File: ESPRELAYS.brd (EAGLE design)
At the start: 47 x 78 mm, 52 parts, among them IC1 ESP12SMT, J1 2.1MM DC Jack, K1 HE751, K2 HE751, K3 HE751, K4 HE751, Q1 2N7002, Q2 2N7002, Q3 2N7002, Q4 2N7002

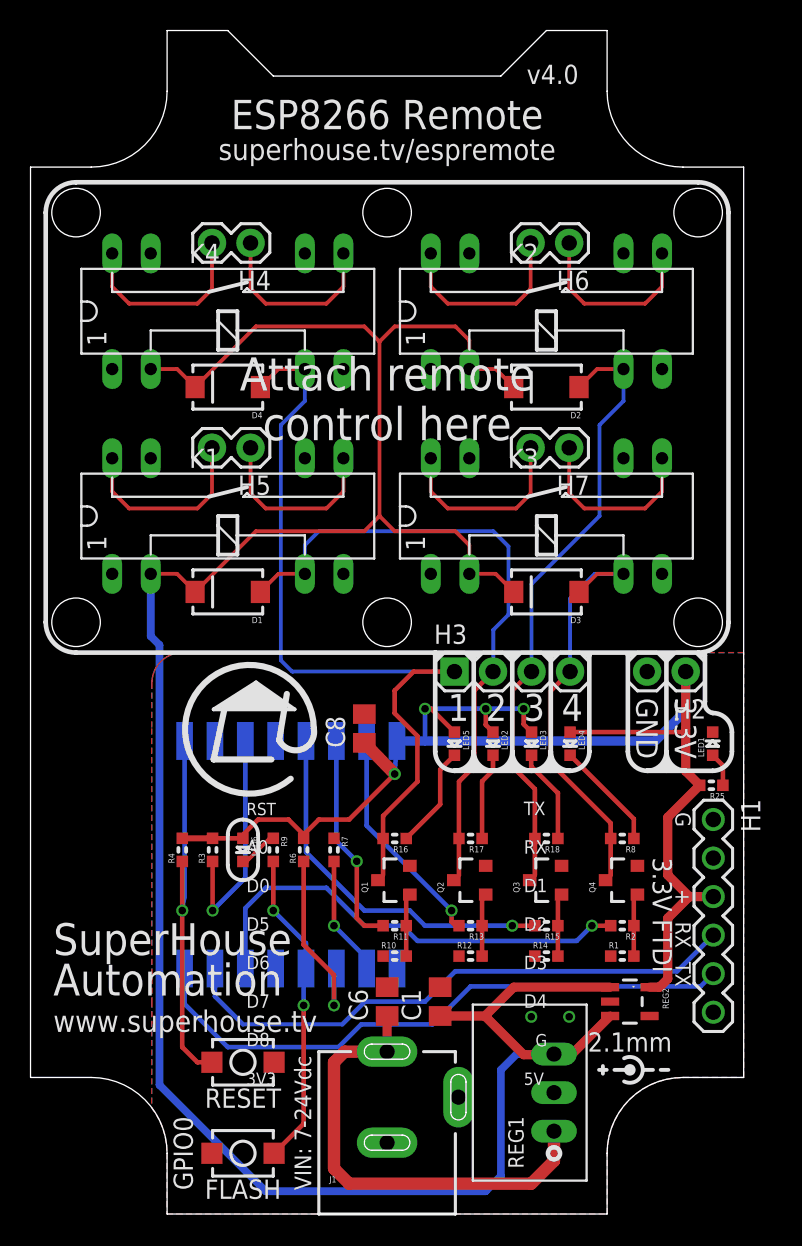
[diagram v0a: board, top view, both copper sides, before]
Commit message: Added SIP reed relays
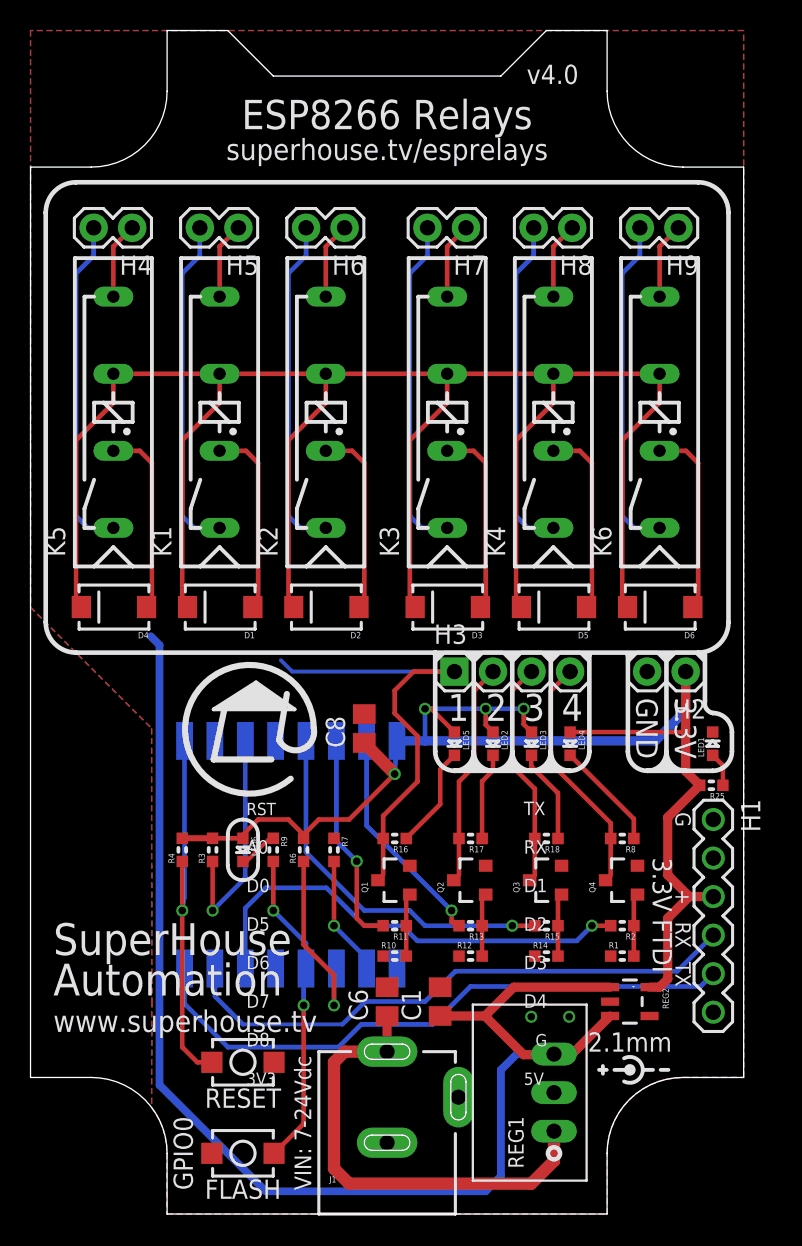
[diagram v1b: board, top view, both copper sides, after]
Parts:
- added D5, D6: (no value), SparkFun:SMA-DIODE
- added H8, H9: (no value), freetronics-jon:1X02
- added K5, K6: REED, relay:REED
- K1, K2, K3, K4: value HE751 -> REED; device relay:HE751 -> relay:REED
- moved K4 24.3 mm to (37.0, 63.0), turned to 90 degrees
- moved D2 20.5 mm to (19.5, 40.0)
- moved K3 17.5 mm to (30.0, 63.0), turned to 90 degrees
- moved K1 17.1 mm to (15.0, 63.0), turned to 90 degrees
- moved D4 16.3 mm to (5.50, 40.0)
- moved H7 16.0 mm to (28.7, 65.0)
- moved H6 14.8 mm to (20.7, 65.0)
- moved H5 14.5 mm to (13.7, 65.0)
- moved K2 12.5 mm to (22.0, 63.0), turned to 90 degrees
- moved H4 7.86 mm to (6.70, 65.0)
- moved D3 6.58 mm to (27.5, 40.0)
- moved D1 1.12 mm to (12.5, 40.0)
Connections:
- new net N$15: H8.1, K4.7
- new net N$16: H8.2, K4.1
- new net N$17: H9.1, K6.7
- new net N$18: H9.2, K6.1
- new net OUT5: D5.A, K4.3
- new net OUT6: D6.A, K6.3
- net 5V: now also D5.C, D6.C, K1.5, K2.5, K3.5, K4.5, K5.5, K6.5; no longer K1.2, K2.2, K3.2, K4.2
- net N$12: now also K5.1; no longer K4.14
- net N$13: now also K3.7; no longer K3.8
- net N$14: now also K3.1; no longer K3.14
- net N$3: now also K1.7; no longer K1.8
- net N$5: now also K1.1; no longer K1.14
- net N$6: now also K2.7; no longer K2.8
- net N$8: now also K5.7; no longer K4.8
- net N$9: now also K2.1; no longer K2.14
- net OUT1: now also K5.3; no longer K4.6
- net OUT2: now also K1.3; no longer K1.6
- net OUT3: now also K2.3; no longer K2.6
- net OUT4: now also K3.3; no longer K3.6
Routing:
- net 5V: track 163.9 -> 224.2 mm
- net N$18: track 0.00 -> 22.3 mm
- net N$16: track 0.00 -> 22.3 mm
- net OUT2: track 43.0 -> 27.4 mm
- net OUT3: track 41.0 -> 27.6 mm
- net OUT6: track 0.00 -> 12.5 mm
- net OUT5: track 0.00 -> 12.5 mm
- net OUT1: track 53.7 -> 42.9 mm
- net N$5: track 12.7 -> 22.3 mm
- net N$12: track 12.7 -> 22.3 mm
- net N$9: track 12.7 -> 22.3 mm
- net N$14: track 12.7 -> 22.3 mm
- net N$3: track 12.2 -> 5.05 mm
- net N$8: track 12.2 -> 5.05 mm
- net N$6: track 12.2 -> 5.05 mm
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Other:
- board text added: "ESP8266 Relays"
- board text added: "superhouse.tv/esprelays"
- board text removed: "Attach remote control here"
- board text removed: "ESP8266 Remote"
- board text removed: "superhouse.tv/espremote"

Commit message: Routing for v1.0 release
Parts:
- removed H2: (no value), freetronics-jon:1X02
- removed H3: (no value), freetronics-jon:1X04
- added JP1: (no value), freetronics-jon:1X03
- added LED7, LED8: RED, freetronics-master-v1:LED-0603
- added Q5, Q6: 2N7002, freetronics-master-v1:SOT23-3
- added R19, R20, R22, R23: 1K, freetronics-master-v1:0603
- added R21, R5: 10K, freetronics-master-v1:0603
- D1, D2, D3, D4, D5, D6: value (none) -> 1N4004
- LED2: value CH2/RED -> RED
- LED3: value CH3/RED -> RED
- LED4: value CH4/RED -> RED
- LED5: value CH1/RED -> RED
- moved R16 39.6 mm to (6.00, 60.0), turned to 0 degrees
- moved R17 38.7 mm to (13.0, 60.0), turned to 0 degrees
- moved R18 37.9 mm to (20.0, 60.0), turned to 0 degrees
- moved LED5 37.6 mm to (6.00, 61.5), turned to 180 degrees
- moved R8 37.2 mm to (27.0, 60.0), turned to 0 degrees
- moved LED2 35.2 mm to (13.0, 61.5), turned to 180 degrees
- moved LED3 33.2 mm to (20.0, 61.5), turned to 180 degrees
- moved LED4 31.7 mm to (27.0, 61.5), turned to 180 degrees
- moved R1 16.3 mm to (27.0, 28.0)
- moved Q4 15.0 mm to (27.0, 31.0)
- moved Q3 14.2 mm to (23.0, 31.0)
- moved R14 14.2 mm to (23.0, 26.0)
- moved R15 14.2 mm to (23.0, 28.0)
- moved R2 13.9 mm to (27.0, 26.0)
- moved Q2 13.5 mm to (19.0, 31.0)
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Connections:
- new net N$19: Q5.1, R19.1, R5.2
- new net N$20: LED7.C, R20.1
- new net N$22: Q6.1, R21.2, R22.1
- new net N$26: LED8.C, R23.1
- net 3.3V: now also JP1.2; no longer H2.1, LED2.A, LED3.A, LED4.A, LED5.A
- net 5V: now also JP1.1, LED2.A, LED3.A, LED4.A, LED5.A, LED7.A, LED8.A
- net GND: now also JP1.3, Q5.2, Q6.2, R21.1, R5.1; no longer H2.2
- net GPIO15: now also R22.2
- net GPIO16: now also R19.2
- net OUT1: no longer H3.1
- net OUT2: no longer H3.2
- net OUT3: no longer H3.3
- net OUT4: no longer H3.4
- net OUT5: now also Q5.3, R20.2
- net OUT6: now also Q6.3, R23.2
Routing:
- net 5V: track 224.2 -> 367.4 mm
- net OUT6: track 12.5 -> 36.5 mm
- net GPIO16: track 0.00 -> 23.6 mm, vias 0 -> 1
- net OUT5: track 12.5 -> 33.5 mm
- net GPIO15: track 7.95 -> 26.0 mm, vias 1 -> 2
- net 3.3V: track 92.8 -> 80.2 mm, vias 4 -> 1
- net GPIO14: track 24.4 -> 12.0 mm
- net OUT2: track 27.4 -> 38.0 mm
- net GPIO5: track 30.5 -> 20.4 mm
- net OUT3: track 27.6 -> 35.3 mm
- net GPIO13: track 14.8 -> 8.93 mm
- net N$11: track 7.25 -> 1.50 mm
- net N$24: track 6.80 -> 1.50 mm
- net N$4: track 6.23 -> 1.50 mm
- net OUT4: track 28.6 -> 33.1 mm
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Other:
- board text added: "(C)2019 SuperHouse Automation Pty Ltd"
- board text added: "5"
- board text added: "6"
- board text added: "Output 1: GPIO12 Output 2: GPIO13 Output 3: GPIO14 Output 4: GPIO5 Output 5: GPIO16 Output 6: GPIO15"
- board text added: "SKU: ESPRELAYS"
- board text added: "v1.0"
- board text removed: "(C)2017 SuperHouse Automation Pty Ltd"
- board text removed: "GND"
- board text removed: "Output 1: GPIO12 Output 2: GPIO13 Output 3: GPIO14 Output 4: GPIO5"
- board text removed: "SKU: ESPREMOTE"
- board text removed: "v4.0"
